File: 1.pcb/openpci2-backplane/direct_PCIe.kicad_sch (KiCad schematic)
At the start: 32 parts, among them J13 1-2199230-6, J14 PCIE-064-02-X-D-TH, J15 10018784-10210TLF, J16 1-2199230-6, U8 TPS563206DRLR, U9 TPS563206DRLR

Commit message: Replaced Clock generator
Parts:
- C66, C77: DigiKey 399-3683-1-ND -> PCE4579CT-ND; Mouser 80-T491A106K0067280 -> 667-EEE-1CA101WAP; TME T491A106K006AT -> EEE1CA101WAP
- JP14, JP15: value ~ -> n/a
- renumbered R26 to R24, R27 to R25, R28 to R26, R29 to R27, R30 to R28, R31 to R29, R32 to R30, R33 to R31, U8 to U7, U9 to U8

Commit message: Schematics update
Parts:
- renumbered C66 to C69, C67 to C70, C68 to C71, C69 to C72, C70 to C73, C71 to C74, C72 to C75, C73 to C76, C74 to C77, C75 to C78, C76 to C79, C77 to C80, U7 to U8, U8 to U9

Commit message: PoL converters added
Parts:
- renumbered C80 to C100, C69 to C89, C70 to C90, C71 to C91, C72 to C92, C73 to C93, C74 to C94, C75 to C95, C76 to C96, C77 to C97, C78 to C98, C79 to C99, J13 to J14, J14 to J15, J15 to J16, J16 to J17, L2 to L6, L3 to L7, R24 to R36, R25 to R37, R26 to R38, R27 to R39, R28 to R40, R29 to R41, R30 to R42, R31 to R43, U8 to U12, U9 to U13

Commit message: Comments updated
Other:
- note added: "1-lane PCIe"
- note added: "2-lane PCIe"
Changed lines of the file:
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@@
 	(paper "A4")
 	(title_block
-		(date "2025-01-29")
+		(date "2025-02-02")
 		(rev "r1B1")
 		(company "Chili.CHIPS")
@@
 		)
 	)
+	(text "2-lane PCIe"
+		(exclude_from_sim no)
+		(at 15.24 17.78 0)
+		(effects
+			(font
+				(size 1.778 1.5113)
+				(color 194 194 194 1)
+			)
+			(justify left bottom)
+		)
+	)
+	(text "1-lane PCIe"
+		(exclude_from_sim no)
+		(at 193.04 17.78 0)
+		(effects
+			(font
+				(size 1.778 1.5113)
+				(color 194 194 194 1)
+			)
+			(justify left bottom)
+		)
+	)

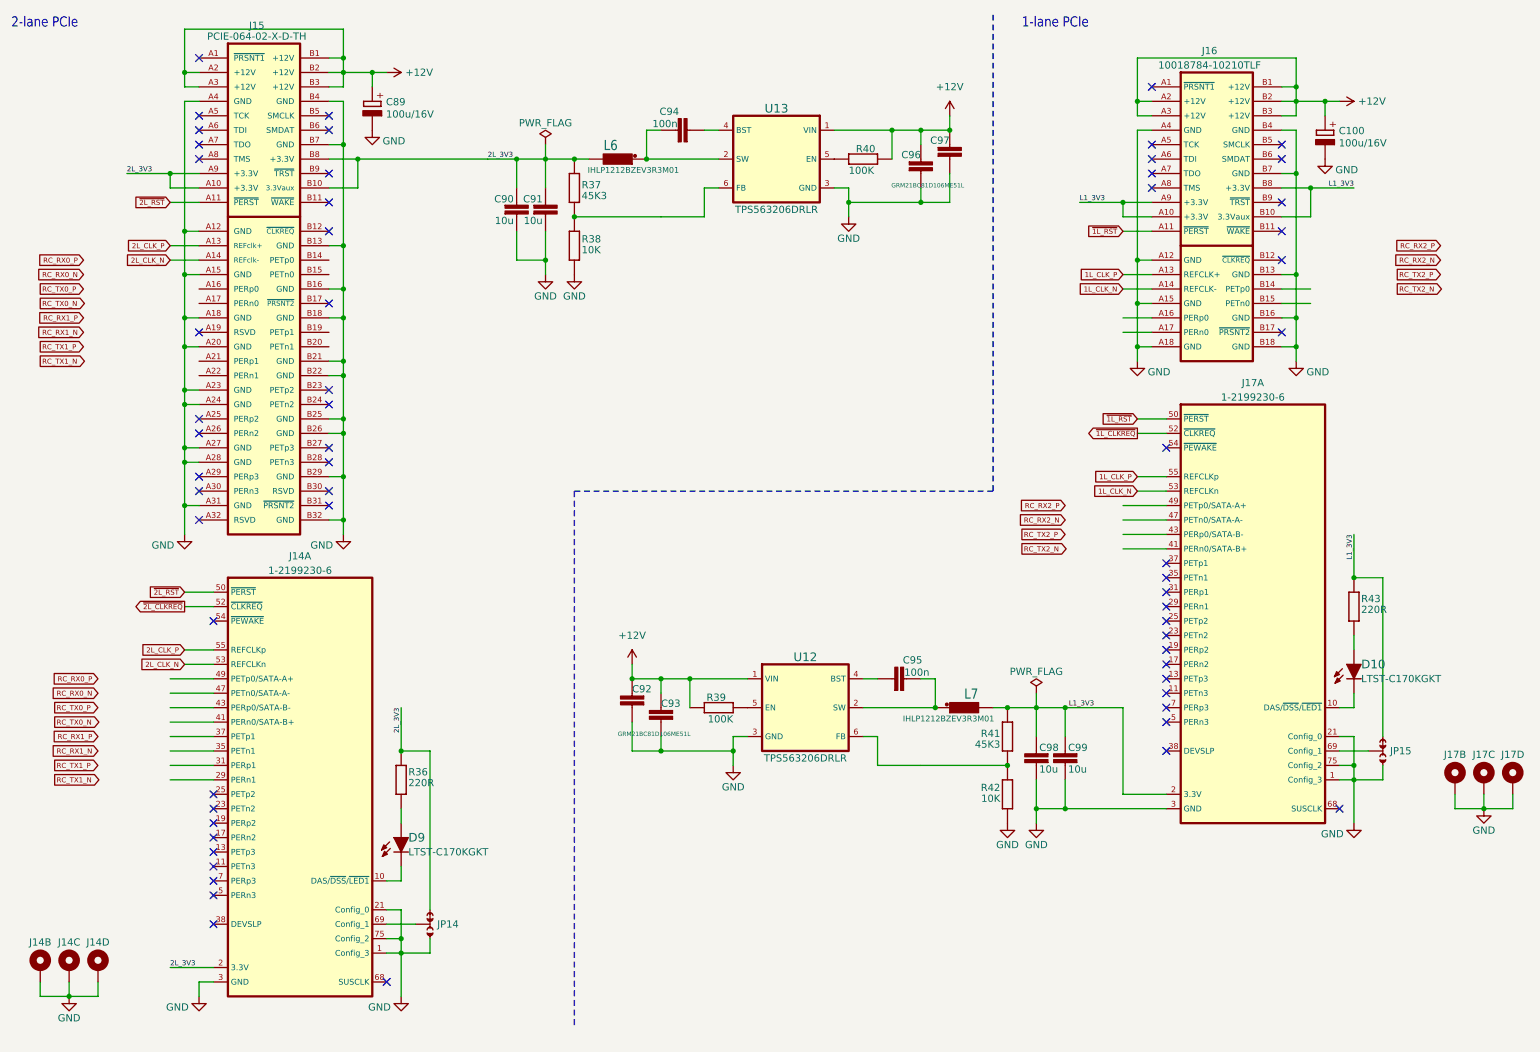
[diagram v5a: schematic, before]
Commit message: PCIe diff lines interconnect, first try
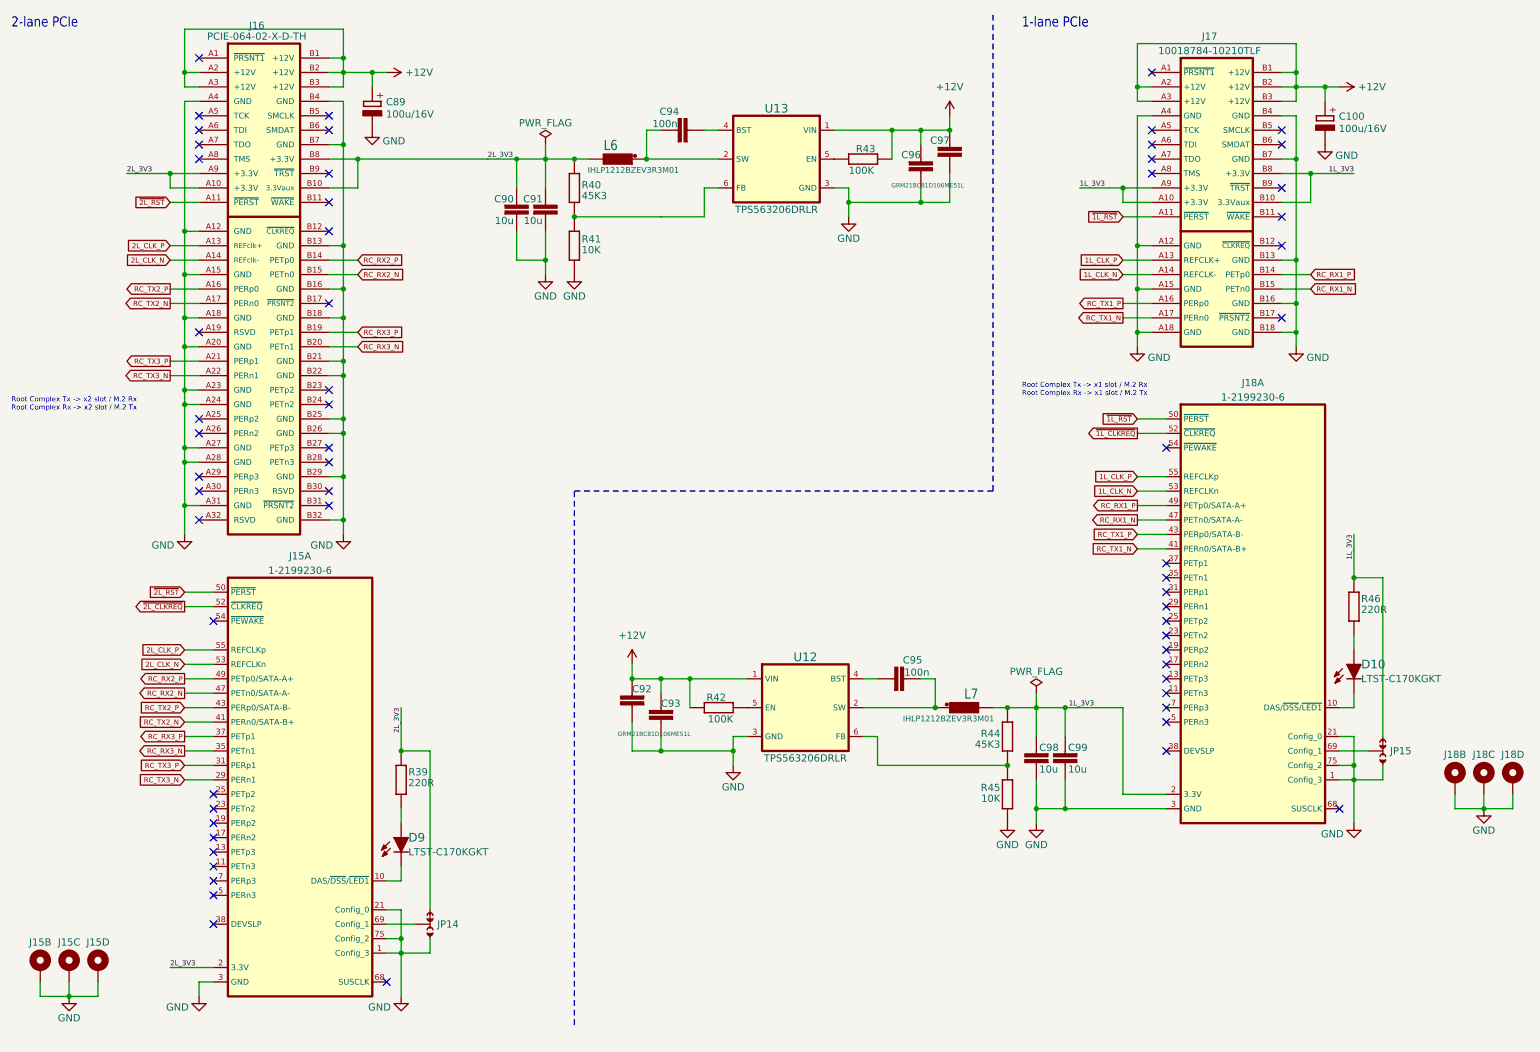
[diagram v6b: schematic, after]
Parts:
- renumbered J14 to J15, J15 to J16, J16 to J17, J17 to J18, R36 to R39, R37 to R40, R38 to R41, R39 to R42, R40 to R43, R41 to R44, R42 to R45, R43 to R46
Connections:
- net RC_RX1_N: now also J17.B15 (PETn0), J18.47 (PETn0/SATA-A-)
- net RC_RX1_P: now also J17.B14 (PETp0), J18.49 (PETp0/SATA-A+)
- net RC_RX2_N: now also J15.47 (PETn0/SATA-A-), J16.B15 (PETn0)
- net RC_RX2_P: now also J15.49 (PETp0/SATA-A+), J16.B14 (PETp0)
- net RC_TX1_N: now also J17.A17 (PERn0), J18.41 (PERn0/SATA-B+)
- net RC_TX1_P: now also J17.A16 (PERp0), J18.43 (PERp0/SATA-B-)
- net RC_TX2_N: now also J15.41 (PERn0/SATA-B+), J16.A17 (PERn0)
- net RC_TX2_P: now also J15.43 (PERp0/SATA-B-), J16.A16 (PERp0)
- net RC_TX3_P: now reaches J16.A21 (PERp1)
- net RC_TX3_P: now also J15.31 (PERp1)
- net RC_TX3_N: now reaches J16.A22 (PERn1)
- net RC_TX3_N: now also J15.29 (PERn1)
- net RC_RX3_P: now reaches J16.B19 (PETp1)
- net RC_RX3_P: now also J15.37 (PETp1)
- net RC_RX3_N: now reaches J16.B20 (PETn1)
- net RC_RX3_N: now also J15.35 (PETn1)
- net L1_3V3 renamed 1L_3V3
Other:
- note added: "Root Complex Tx -> x1 slot / M.2 Rx Root Complex Rx -> x1 slot / M.2 Tx"
- note added: "Root Complex Tx -> x2 slot / M.2 Rx Root Complex Rx -> x2 slot / M.2 Tx"
- moved on the sheet: C100, J17

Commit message: Few small changes
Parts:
- J18: renamed from J16; value PCIE-064-02-X-D-TH -> 10018784-10201TLF; DigiKey (none) -> 609-2026-ND; Mouser (none) -> 649-1001878410201TLF; TME (none) -> 1001878410201T-0
- renumbered J15 to J17, J17 to J19, J18 to J20, R39 to R38, R40 to R39, R41 to R40, R42 to R41, R43 to R42, R44 to R43, R45 to R44, R46 to R45
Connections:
- net GND: now also J17.GND1 (Gnd), J17.GND2 (Gnd), J17.GND3 (Gnd), J20.GND1 (Gnd), J20.GND2 (Gnd), J20.GND3 (Gnd); no longer J17.GND (Gnd), J17.GND (Gnd), J17.GND (Gnd), J20.GND (Gnd), J20.GND (Gnd), J20.GND (Gnd)

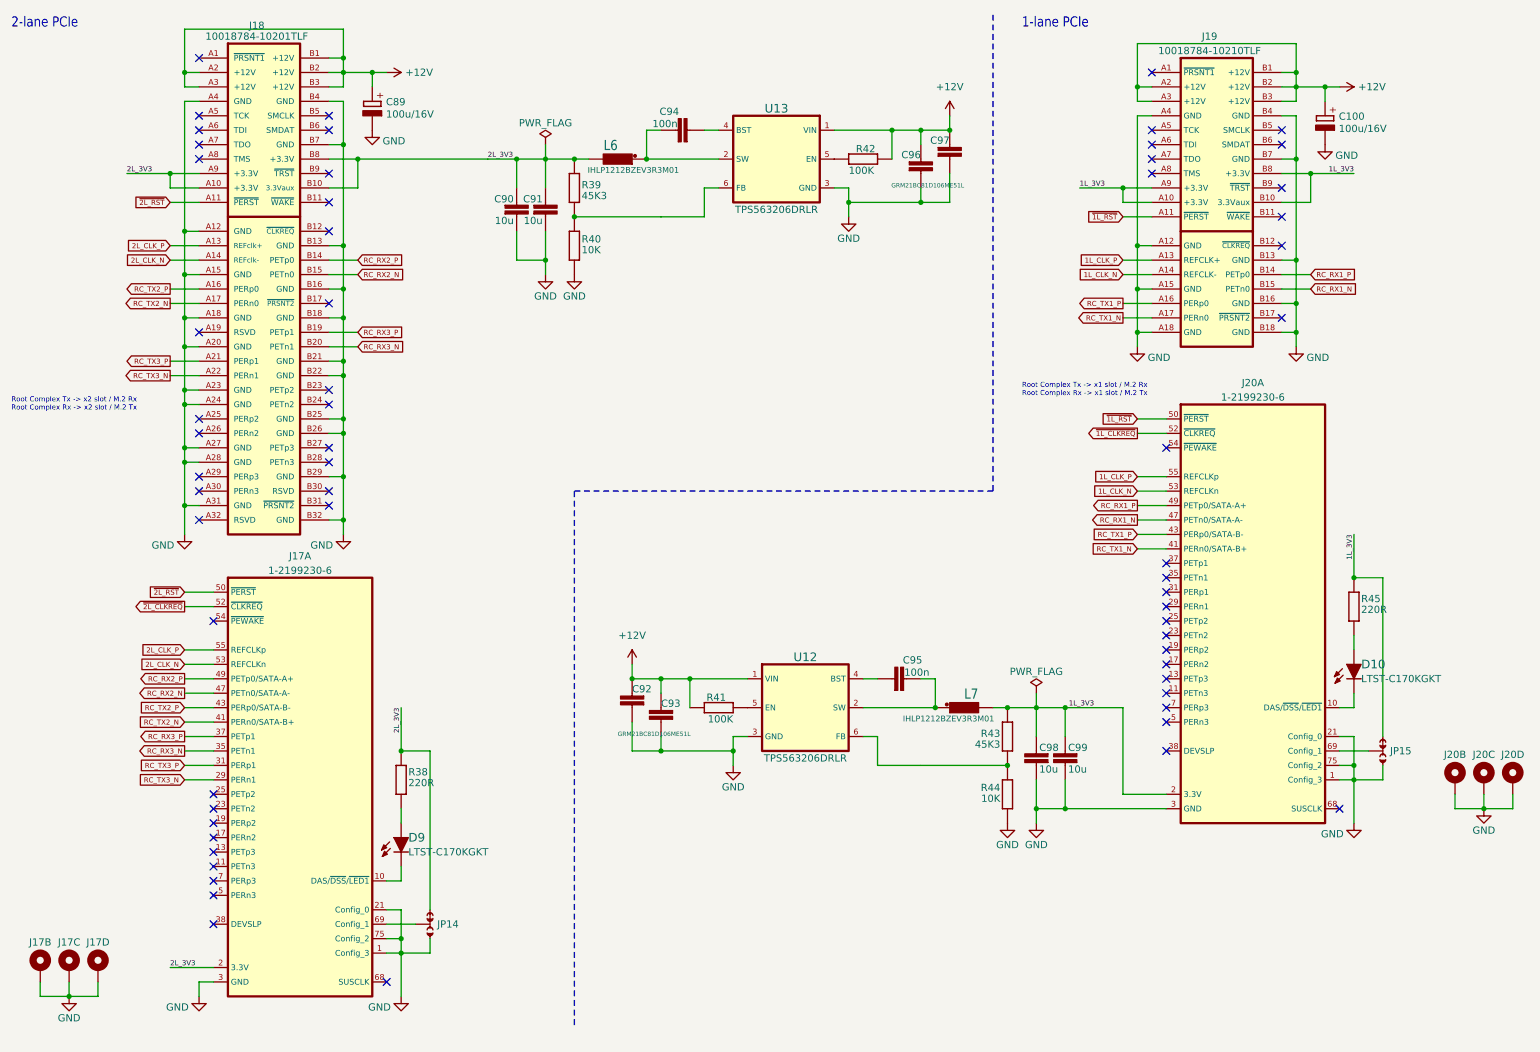
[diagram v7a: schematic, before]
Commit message: 3V3 power rails consolidation
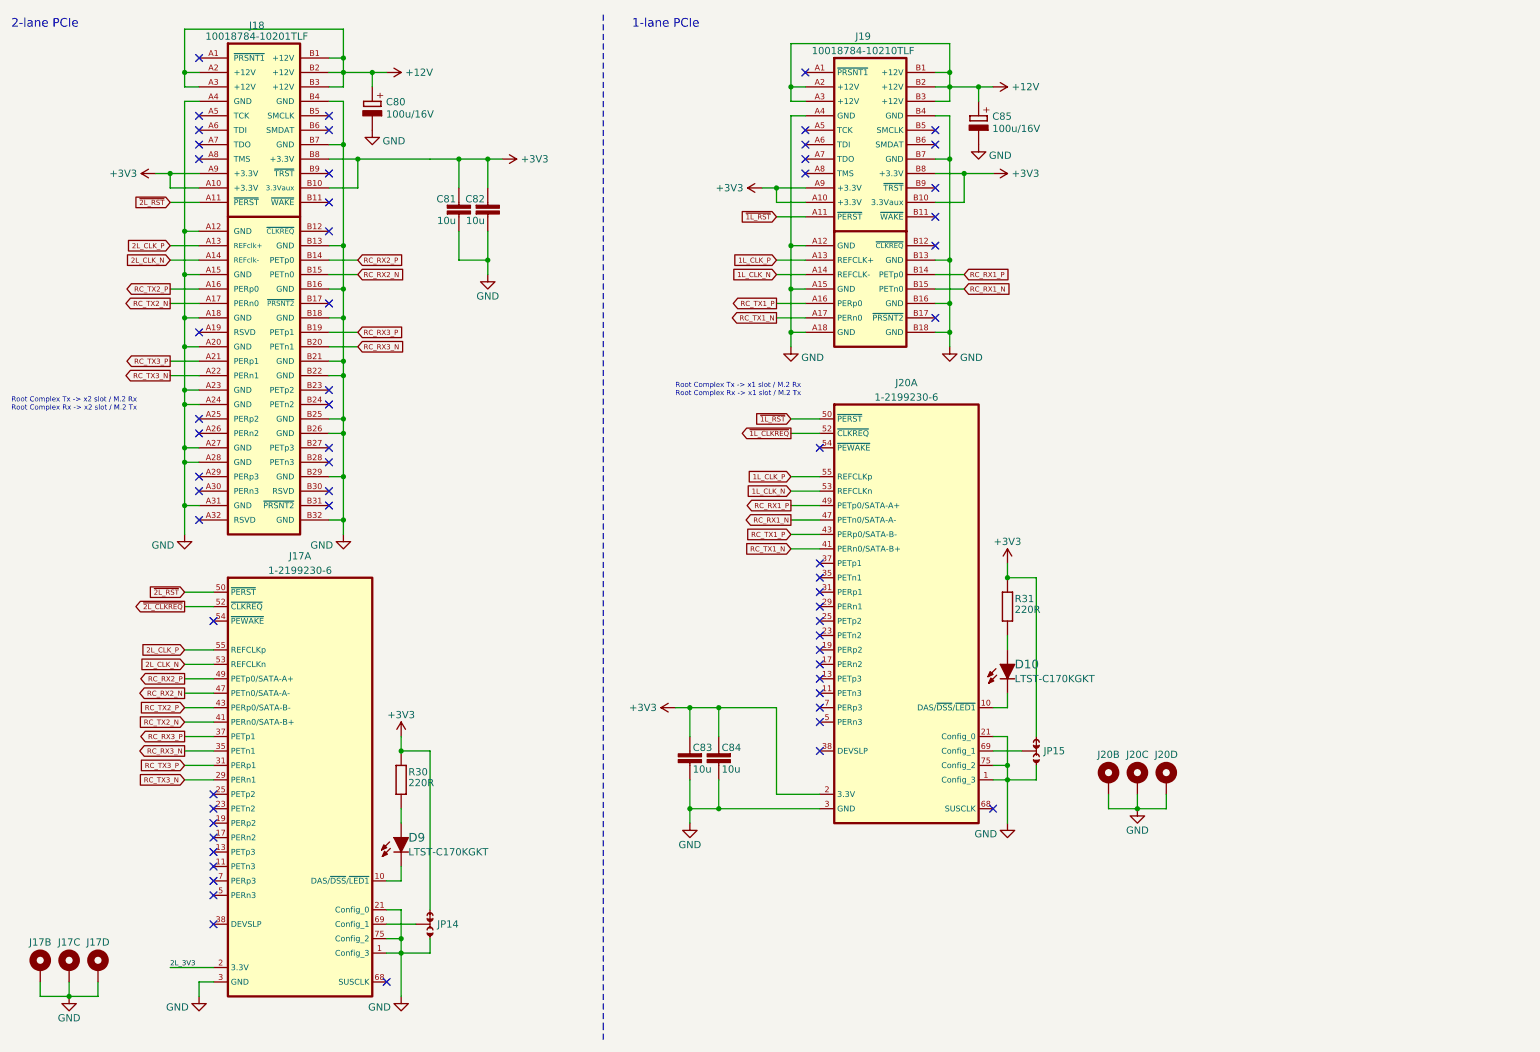
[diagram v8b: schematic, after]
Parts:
- removed C92, C93, C96, C97: GRM21BC81D106ME51L, PCM_EEZ_passives:C_0805_2012Metric, symbol PCM_EEZ_passives:C-EU
- removed C94, C95: 100n, PCM_EEZ_passives:C_0603_1608Metric, symbol PCM_EEZ_passives:C-EU
- removed L6, L7: IHLP1212BZEV3R3M01, PCM_Chili-chips:IND_IHLP1212BZER3R3M11, symbol PCM_EEZ_passives:L_EU_polarised
- removed R39, R43: 45K3, PCM_EEZ_passives:R_0603_1608Metric, symbol PCM_EEZ_passives:R-EU
- removed R40, R44: 10K, PCM_EEZ_passives:R_0603_1608Metric, symbol PCM_EEZ_passives:R-EU
- removed R41, R42: 100K, PCM_EEZ_passives:R_0603_1608Metric, symbol PCM_EEZ_passives:R-EU
- removed U12, U13: TPS563206DRLR, PCM_Chili-chips:SOT_07SDRLR_TEX-L, symbol PCM_Chili-chips:TPS563202DRLR
- renumbered C89 to C80, C90 to C81, C91 to C82, C98 to C83, C99 to C84, C100 to C85, R38 to R30, R45 to R31
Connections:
- net 2L_3V3: no longer C81.2, C82.2, J18.A10 (+3.3V), J18.A9 (+3.3V), J18.B10 (3.3Vaux), J18.B8 (+3.3V), JP14.NC, R30.1
- net 1L_3V3 renamed +3V3
- net +3V3: now also C81.2, C82.2, J18.A10 (+3.3V), J18.A9 (+3.3V), J18.B10 (3.3Vaux), J18.B8 (+3.3V), JP14.NC, R30.1
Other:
- moved on the sheet: C81, C82, C83, C84, C85, D10, J19, J20A, J20B, J20C, J20D, JP15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
